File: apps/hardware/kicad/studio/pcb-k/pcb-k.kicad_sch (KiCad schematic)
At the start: 46 parts, among them J1 A PCB-A (JST-SH 10), SW1 B1 OSC/INSERT, SW2 B2 ENV/SEND, SW3 B3 LFO/MASTER, SW4 B4 PRESET/FAV, SW5 B5 MODE, SW6 B6 HOLD/SHIFT

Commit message: feat(hardware): esquemático de la portadora de Studio y ajuste del apilado del panel
Portadora (rev 0.1, ERC sin violaciones):
- USB-C 5 V solo alimentación (CC 5.1 kΩ), polyfuse 3 A, TVS y bulk; VIN de la
  Teensy con el puente VUSB–VIN cortado.
- Teensy 4.1 como dos filas de 24 pines; USB host a USB-A; IDC 2×15 al panel con
  el mismo pinout de PCB-A; IDC 2×5 a los pines 1–10 de la Pi (5 V y UART).
- LEDs: pin 28 → 74AHCT1G125 a 5 V → puente de soldadura (saltar el buffer) → 330 Ω.
- Entrada estéreo: escalera 0/−10/−20 dB con palanca DP3T, acople, protección
  BAT54S sobre VREF de 1.65 V y seguidores MCP6004 hacia LINE IN del Audio Shield.
- Salidas 6.35 con acople, PHONES 3.5 con el sleeve en HP_VGND, CV OUT con RC de
  2 polos y seguidor.

Apilado del panel: PCB-A baja a −12.0 mm con separadores M3 estándar de 10 mm (buje
al ras, eje a 14.5 mm), PCB-K con agujeros de 8.0 mm y cuelga de los Choc, JST-SH de
entrada lateral entre placas. El pad estéreo no se lee (pin 25 libre).

Co-Authored-By: Claude Opus 5.5 <noreply@anthropic.com>
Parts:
- J1: footprint Connector_JST:JST_SH_BM10B-SRSS-TB_1x10-1MP_P1.00mm_Vertical -> Connector_JST:JST_SH_SM10B-SRSS-TB_1x10-1MP_P1.00mm_Horizontal
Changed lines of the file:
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@@
 			)
 		)
-		(property "Footprint" "Connector_JST:JST_SH_BM10B-SRSS-TB_1x10-1MP_P1.00mm_Vertical"
+		(property "Footprint" "Connector_JST:JST_SH_SM10B-SRSS-TB_1x10-1MP_P1.00mm_Horizontal"
 			(at 15.24 90.17 0)
 			(hide yes)

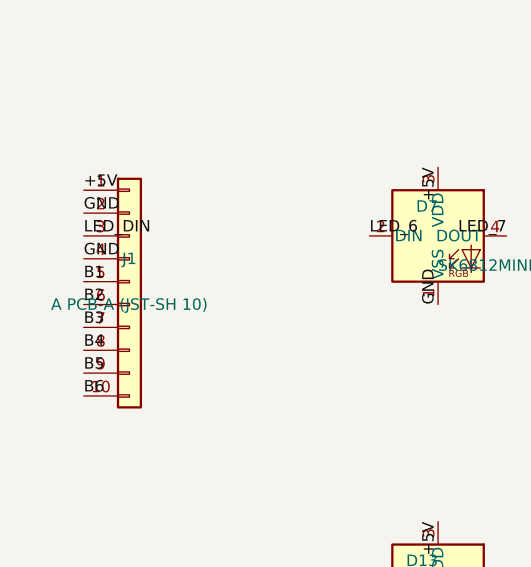
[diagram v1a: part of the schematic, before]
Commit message: feat(hardware): PCB-K ruteada (DRC limpio contra reglas de JLCPCB)
- Anillo de NAV: LEDs rotados 180° para que DOUT y DIN queden enfrentados en cada hueco (mismo
  orden e índices 0–11). Ruteo regular por script: anillo interior de +5V, saltos de datos por F.Cu
  que esquivan las ventanas de luz, una vía de GND por hueco (tools/route_pcb_k_ring.py).
- Zona de teclas con rutas explícitas (tools/route_pcb_k_keys.py): botones por F.Cu desde J1,
  cadena de datos y buses de +5V por B.Cu; capacitores de tecla a la derecha de cada LED; C19 sobre
  el bus de +5V; TP1/TP2 sobre sus pistas y fuera del BOM.
- Orden de pines de J1 nuevo en PCB-K y PCB-A (cable 1:1): B4, B6, B3, GND, +5V, GND, LED_DIN, B2,
  B5, B1. Evita ~14 cruces entre capas; los pines de la Teensy no cambian (02-studio-pcb.md §6.1).
- Planos de GND en F.Cu y B.Cu con costura cada 6 mm (tools/add_gnd_pours.py).
- Reglas de JLCPCB 2 capas en los tres proyectos: agujero-agujero 0.5 mm, vía ≥ 0.5/0.3, anillo
  ≥ 0.13; borde 0.25 mm (0.2 solo dentro de cada SK6812MINI-E).
- DRC con paridad de esquemático: 0 violaciones, 0 pads sin conectar, 0 errores de footprint.
- tools/route_board.py (Freerouting) queda como herramienta; no se usó en el resultado final.

Co-Authored-By: Claude Opus 5.5 <noreply@anthropic.com>
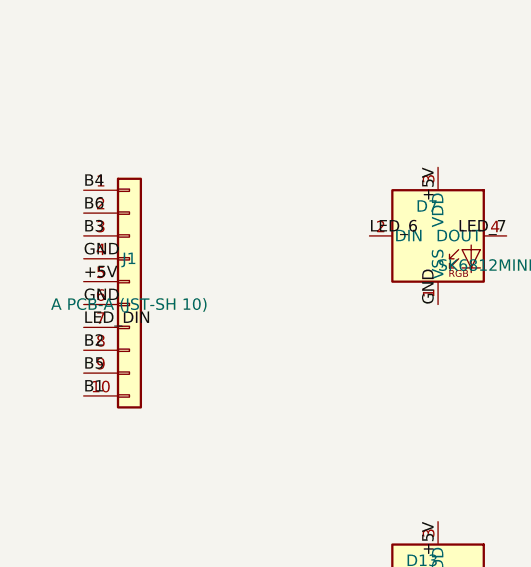
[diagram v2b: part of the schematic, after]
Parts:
- TP1, TP2: now left out of the parts list
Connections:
- net +5V: now also J1.5 (Pin_5); no longer J1.1 (Pin_1)
- net B1: now also J1.10 (Pin_10); no longer J1.5 (Pin_5)
- net B2: now also J1.8 (Pin_8); no longer J1.6 (Pin_6)
- net B3: now also J1.3 (Pin_3); no longer J1.7 (Pin_7)
- net B4: now also J1.1 (Pin_1); no longer J1.8 (Pin_8)
- net B6: now also J1.2 (Pin_2); no longer J1.10 (Pin_10)
- net GND: now also J1.6 (Pin_6); no longer J1.2 (Pin_2)
- net LED_DIN: now also J1.7 (Pin_7); no longer J1.3 (Pin_3)
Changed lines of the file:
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@@
 		(body_style 1)
 		(exclude_from_sim no)
-		(in_bom yes)
+		(in_bom no)
 		(on_board yes)
 		(in_pos_files yes)
@@
 		(body_style 1)
 		(exclude_from_sim no)
-		(in_bom yes)
+		(in_bom no)
 		(on_board yes)
 		(in_pos_files yes)
@@
 			)
 			(justify right bottom)
-		)
-	)
-	(label "+5V"
-		(at 10.16 80.01 0)
-		(effects
-			(font
-				(size 1.27 1.27)
-			)
-			(justify left bottom)
-		)
-	)
-	(label "GND"
-		(at 10.16 82.55 0)
-		(effects
-			(font
-				(size 1.27 1.27)
-			)
-			(justify left bottom)
-		)
-	)
-	(label "LED_DIN"
-		(at 10.16 85.09 0)
-		(effects
-			(font
-				(size 1.27 1.27)
-			)
-			(justify left bottom)
-		)
-	)
-	(label "GND"
-		(at 10.16 87.63 0)
-		(effects
-			(font
-				(size 1.27 1.27)
-			)
-			(justify left bottom)
-		)
-	)
-	(label "B1"
-		(at 10.16 90.17 0)
-		(effects
-			(font
-				(size 1.27 1.27)
-			)
-			(justify left bottom)
-		)
-	)
-	(label "B2"
-		(at 10.16 92.71000000000001 0)
-		(effects
-			(font
-				(size 1.27 1.27)
-			)
-			(justify left bottom)
-		)
-	)
-	(label "B3"
-		(at 10.16 95.25 0)
-		(effects
-			(font
-				(size 1.27 1.27)
-			)
-			(justify left bottom)
-		)
-	)
-	(label "B4"
-		(at 10.16 97.79 0)
-		(effects
-			(font
-				(size 1.27 1.27)
-			)
-			(justify left bottom)
-		)
-	)
-	(label "B5"
-		(at 10.16 100.33 0)
-		(effects
-			(font
-				(size 1.27 1.27)
-			)
-			(justify left bottom)
-		)
-	)
-	(label "B6"
-		(at 10.16 102.87 0)
-		(effects
-			(font
-				(size 1.27 1.27)
-			)
-			(justify left bottom)
 		)
 	)
@@
 			)
 			(justify left bottom)
+		)
+	)
+	(label "B4"
+		(at 10.16 80.01 0)
+		(effects
+			(font
+				(size 1.27 1.27)
+			)
+			(justify left bottom)
+		)
+	)
+	(label "B6"
+		(at 10.16 82.55 0)
+		(effects
+			(font
+				(size 1.27 1.27)
+			)
+			(justify left bottom)
+		)
+	)
+	(label "B3"
+		(at 10.16 85.09 0)
+		(effects
+			(font
+				(size 1.27 1.27)
+			)
+			(justify left bottom)
+		)
+	)
+	(label "GND"
+		(at 10.16 87.63 0)
+		(effects
+			(font
+				(size 1.27 1.27)
+			)
+			(justify left bottom)
+		)
+	)
+	(label "+5V"
+		(at 10.16 90.17 0)
+		(effects
+			(font
+				(size 1.27 1.27)
+			)
+			(justify left bottom)
+		)
+	)
+	(label "GND"
+		(at 10.16 92.71000000000001 0)
+		(effects
+			(font
+				(size 1.27 1.27)
+			)
+			(justify left bottom)
+		)
+	)
+	(label "LED_DIN"
+		(at 10.16 95.25 0)
+		(effects
+			(font
+				(size 1.27 1.27)
+			)
+			(justify left bottom)
+		)
+	)
+	(label "B2"
+		(at 10.16 97.79 0)
+		(effects
+			(font
+				(size 1.27 1.27)
+			)
+			(justify left bottom)
+		)
+	)
+	(label "B5"
+		(at 10.16 100.33 0)
+		(effects
+			(font
+				(size 1.27 1.27)
+			)
+			(justify left bottom)
+		)
+	)
+	(label "B1"
+		(at 10.16 102.87 0)
+		(effects
+			(font
+				(size 1.27 1.27)
+			)
+			(justify left bottom)

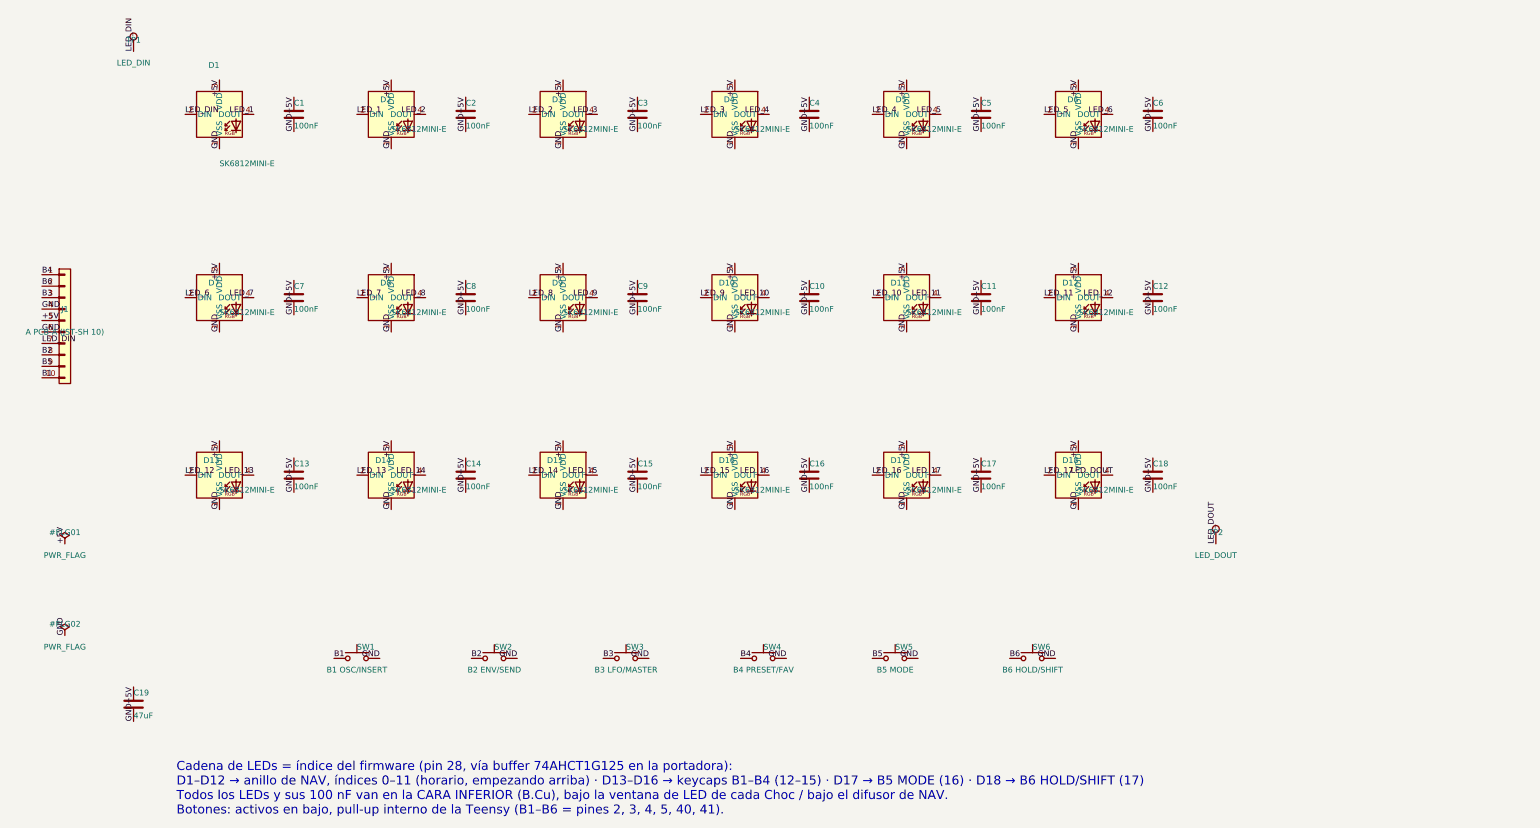
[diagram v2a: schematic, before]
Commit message: feat(hardware): archivos de fabricación JLCPCB y shield corregido en la portadora
- Portadora: las filas del Audio Shield estaban al revés (quedaba espejado respecto de la Teensy con el
  shield boca arriba). J16 (GND/0–12) pasa atrás y J15 adelante; re-ruteada, DRC con paridad 0/0/0.
- Números LCSC en los tres esquemáticos (set_lcsc.py), todo en ensamble Economic. PCB-K pasa al
  SK6812MINI-EA (mismo pinout y cuerpo, sin la restricción Standard-only del MINI-E).
- Escalera del PAD y acople al codec con valores Basic (33k/12k/5.1k, 4.7 µF): la simulación sigue
  pasando C1–C6 (tercera corrida en theory/03).
- export_fab.py: Gerbers + taladros, BOM y CPL en formato JLC; los THT usan el centro de sus pads y los
  IDC la rotación del modelo de JLC. Portadora con jacks e IDC ensamblados; el resto de los THT en
  fab/lcsc-piezas-sueltas.csv.
- sync_fp_fields.py también copia Value y LCSC a las placas.
- theory/02 §10C–10D: fabricación, montaje del shield, J9, J3 (USB host), corriente de la Pi y la
  verificación de punta a punta de las conexiones.

Co-Authored-By: Claude Opus 5.5 <noreply@anthropic.com>
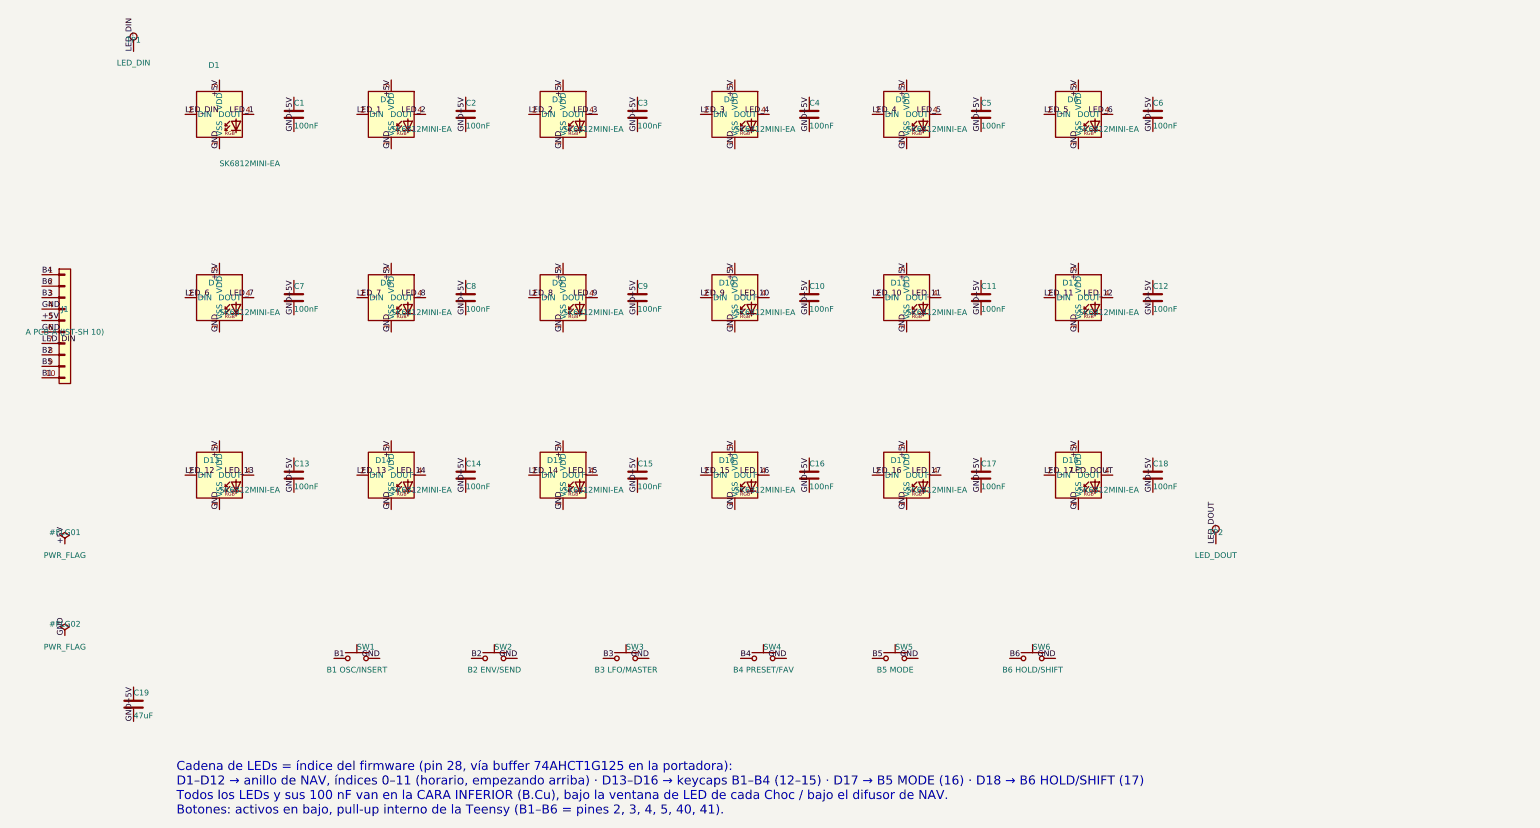
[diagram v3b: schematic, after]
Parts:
- C1, C10, C11, C12, C13, C14, C15, C16, C17, C18, C2, C3, C4, C5, C6, C7, C8, C9: LCSC (none) -> C14663
- C19: LCSC (none) -> C96123
- D1, D10, D11, D12, D13, D14, D15, D16, D17, D18, D2, D3, D4, D5, D6, D7, D8, D9: value SK6812MINI-E -> SK6812MINI-EA; LCSC (none) -> C5378731
- J1: LCSC (none) -> C160409
